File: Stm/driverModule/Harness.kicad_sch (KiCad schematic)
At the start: 2 parts, among them J1 346916080, J3 346916080

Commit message: Update
Add connection to the harness
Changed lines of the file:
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@@
-	(wire
-		(pts
-			(xy 124.46 107.95) (xy 129.54 107.95)
-		)
-		(stroke
-			(width 0)
-			(type default)
-		)
-	)
 	(wire
 		(pts
@@
 	(wire
 		(pts
+			(xy 129.54 107.95) (xy 124.46 107.95)
+		)
+		(stroke
+			(width 0)
+			(type default)
+		)
+	)
+	(wire
+		(pts
 			(xy 124.46 62.23) (xy 129.54 62.23)
+		)
+		(stroke
+			(width 0)
+			(type default)
+		)
+	)
+	(wire
+		(pts
+			(xy 129.54 113.03) (xy 129.54 107.95)
 		)
 		(stroke
@@
 	(hierarchical_label "LIN_BUS"
 		(shape bidirectional)
-		(at 186.69 90.17 0)
+		(at 87.63 86.36 0)
 		(effects
 			(font
@@
 		(shape output)
 		(at 129.54 74.93 0)
+		(effects
+			(font
+				(size 1.27 1.27)
+			)
+			(justify left)
+		)
+	)
+	(hierarchical_label "GND"
+		(shape bidirectional)
+		(at 129.54 107.95 0)
 		(effects
 			(font
@@
 	(symbol
 		(lib_id "power:GND")
-		(at 129.54 107.95 0)
+		(at 129.54 113.03 0)
 		(unit 1)
 		(exclude_from_sim no)
@@
 		(fields_autoplaced yes)
 		(property "Reference" "#PWR019"
-			(at 129.54 114.3 0)
+			(at 129.54 119.38 0)
 			(effects
 				(font
@@
 		)
 		(property "Value" "GND"
+			(at 129.54 118.11 0)
+			(effects
+				(font
+					(size 1.27 1.27)
+				)
+			)
+		)
+		(property "Footprint" ""
 			(at 129.54 113.03 0)
 			(effects
@@
 					(size 1.27 1.27)
 				)
-			)
-		)
-		(property "Footprint" ""
-			(at 129.54 107.95 0)
-			(effects
-				(font
-					(size 1.27 1.27)
-				)
 				(hide yes)
 			)
 		)
 		(property "Datasheet" ""
-			(at 129.54 107.95 0)
+			(at 129.54 113.03 0)
 			(effects
 				(font
@@
 		)
 		(property "Description" "Power symbol creates a global label with name \"GND\" , ground"
-			(at 129.54 107.95 0)
-			(effects
-				(font
+			(at 129.54 113.03 0)
+			(effects
+				(font

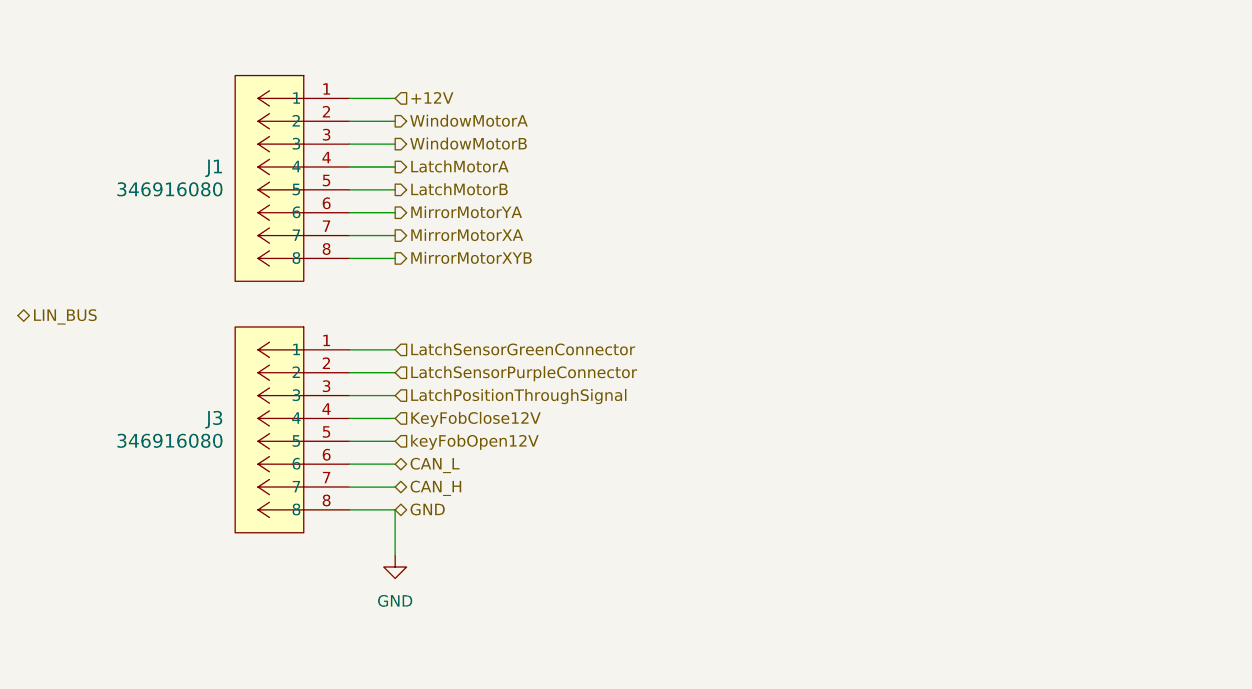
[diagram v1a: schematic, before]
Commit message: libraries
Add new molex connectors
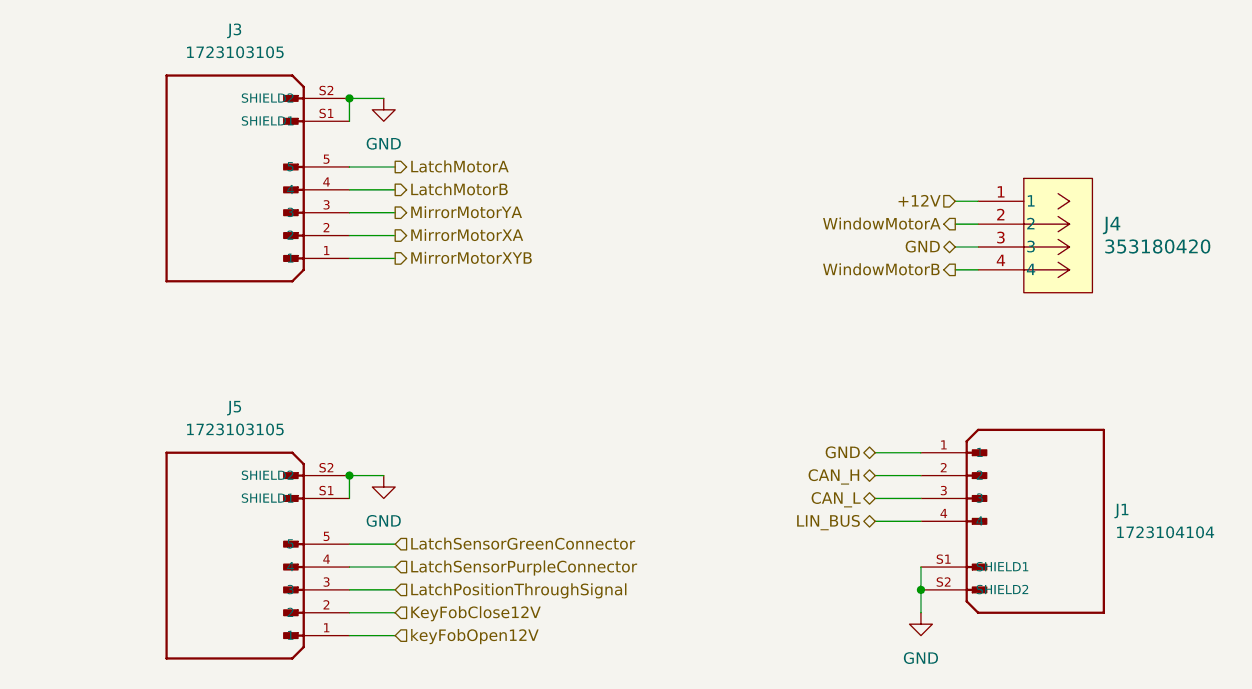
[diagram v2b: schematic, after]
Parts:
- removed J1, J3: 346916080, User_Footprint:CONN_SD-34691-601_08_MOL, symbol _Connectors:346916080
- added J1: 1723104104, User_Footprint:MOLEX_1723104104, symbol _Connectors:1723104104
- added J3, J5: 1723103105, User_Footprint:MOLEX_1723103105, symbol _Connectors:1723103105
- added J4: 353180420, User_Footprint:CONN_35318-0420_MOL, symbol _Misc_Symbols:353180420
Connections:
- net +12V: now also J4.1
- net CAN_H: now also J1.2
- net CAN_L: now also J1.3
- net GND: now also J1.1, J1.S1 (SHIELD1), J1.S2 (SHIELD2), J3.S1 (SHIELD1), J3.S2 (SHIELD2), J4.3, J5.S1 (SHIELD1), J5.S2 (SHIELD2)
- net KeyFobClose12V: now also J5.2
- net LIN_BUS: now also J1.4
- net LatchMotorA: now also J3.5
- net LatchMotorB: now also J3.4
- net LatchPositionThroughSignal: now also J5.3
- net LatchSensorGreenConnector: now also J5.5
- net LatchSensorPurpleConnector: now also J5.4
- net MirrorMotorXA: now also J3.2
- net MirrorMotorXYB: now also J3.1
- net MirrorMotorYA: now also J3.3
- net WindowMotorA: now also J4.2
- net WindowMotorB: now also J4.4
- net keyFobOpen12V: now also J5.1

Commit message: routing
Finished PCB routing
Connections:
- net LatchMotorA: now also J3.4; no longer J3.5
- net LatchMotorB: now also J3.5; no longer J3.4
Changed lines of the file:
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@@
+	(wire
+		(pts
+			(xy 124.46 116.84) (xy 129.54 116.84)
+		)
+		(stroke
+			(width 0)
+			(type default)
+		)
+	)
+	(wire
+		(pts
+			(xy 191.77 73.66) (xy 194.31 73.66)
+		)
+		(stroke
+			(width 0)
+			(type default)
+		)
+	)
+	(wire
+		(pts
+			(xy 187.96 116.84) (xy 187.96 114.3)
+		)
+		(stroke
+			(width 0)
+			(type default)
+		)
+	)
+	(wire
+		(pts
+			(xy 124.46 114.3) (xy 129.54 114.3)
+		)
+		(stroke
+			(width 0)
+			(type default)
+		)
+	)
+	(wire
+		(pts
+			(xy 124.46 77.47) (xy 129.54 77.47)
+		)
+		(stroke
+			(width 0)
+			(type default)
+		)
+	)
+	(wire
+		(pts
+			(xy 187.96 106.68) (xy 182.88 106.68)
+		)
+		(stroke
+			(width 0)
+			(type default)
+		)
+	)
+	(wire
+		(pts
+			(xy 124.46 80.01) (xy 129.54 80.01)
+		)
+		(stroke
+			(width 0)
+			(type default)
+		)
+	)
+	(wire
+		(pts
+			(xy 124.46 119.38) (xy 129.54 119.38)
+		)
+		(stroke
+			(width 0)
+			(type default)
+		)
+	)
+	(wire
+		(pts
+			(xy 124.46 62.23) (xy 124.46 64.77)
+		)
+		(stroke
+			(width 0)
+			(type default)
+		)
+	)
 	(wire
 		(pts
@@
 	(wire
 		(pts
-			(xy 124.46 116.84) (xy 129.54 116.84)
-		)
-		(stroke
-			(width 0)
-			(type default)
-		)
-	)
-	(wire
-		(pts
-			(xy 191.77 73.66) (xy 194.31 73.66)
-		)
-		(stroke
-			(width 0)
-			(type default)
-		)
-	)
-	(wire
-		(pts
-			(xy 187.96 116.84) (xy 187.96 114.3)
-		)
-		(stroke
-			(width 0)
-			(type default)
-		)
-	)
-	(wire
-		(pts
-			(xy 124.46 114.3) (xy 129.54 114.3)
-		)
-		(stroke
-			(width 0)
-			(type default)
-		)
-	)
-	(wire
-		(pts
-			(xy 124.46 77.47) (xy 129.54 77.47)
-		)
-		(stroke
-			(width 0)
-			(type default)
-		)
-	)
-	(wire
-		(pts
-			(xy 187.96 106.68) (xy 182.88 106.68)
-		)
-		(stroke
-			(width 0)
-			(type default)
-		)
-	)
-	(wire
-		(pts
-			(xy 124.46 80.01) (xy 129.54 80.01)
-		)
-		(stroke
-			(width 0)
-			(type default)
-		)
-	)
-	(wire
-		(pts
-			(xy 124.46 119.38) (xy 129.54 119.38)
-		)
-		(stroke
-			(width 0)
-			(type default)
-		)
-	)
-	(wire
-		(pts
-			(xy 124.46 62.23) (xy 124.46 64.77)
-		)
-		(stroke
-			(width 0)
-			(type default)
-		)
-	)
-	(wire
-		(pts
 			(xy 187.96 104.14) (xy 182.88 104.14)
 		)
@@
 	(wire
 		(pts
+			(xy 182.88 101.6) (xy 187.96 101.6)
+		)
+		(stroke
+			(width 0)
+			(type default)
+		)
+	)
+	(wire
+		(pts
+			(xy 124.46 104.14) (xy 124.46 106.68)
+		)
+		(stroke
+			(width 0)
+			(type default)
+		)
+	)
+	(wire
+		(pts
+			(xy 187.96 119.38) (xy 187.96 116.84)
+		)
+		(stroke
+			(width 0)
+			(type default)
+		)
+	)
+	(wire
+		(pts
+			(xy 191.77 81.28) (xy 194.31 81.28)
+		)
+		(stroke
+			(width 0)
+			(type default)
+		)
+	)
+	(wire
+		(pts
 			(xy 124.46 69.85) (xy 129.54 69.85)
 		)
@@
 	(wire
 		(pts
-			(xy 182.88 101.6) (xy 187.96 101.6)
-		)
-		(stroke
-			(width 0)
-			(type default)
-		)
-	)
-	(wire
-		(pts
-			(xy 124.46 104.14) (xy 124.46 106.68)
-		)
-		(stroke
-			(width 0)
-			(type default)
-		)
-	)
-	(wire
-		(pts
-			(xy 187.96 119.38) (xy 187.96 116.84)
-		)
-		(stroke
-			(width 0)
-			(type default)
-		)
-	)
-	(wire
-		(pts
-			(xy 191.77 81.28) (xy 194.31 81.28)
-		)
-		(stroke
-			(width 0)
-			(type default)
-		)
-	)
-	(wire
-		(pts
 			(xy 124.46 74.93) (xy 129.54 74.93)
 		)
@@
 	(hierarchical_label "LatchMotorA"
 		(shape output)
+		(at 129.54 72.39 0)
+		(effects
+			(font
+				(size 1.27 1.27)
+			)
+			(justify left)
+		)
+	)
+	(hierarchical_label "LIN_BUS"
+		(shape bidirectional)
+		(at 182.88 109.22 180)
+		(effects
+			(font
+				(size 1.27 1.27)
+			)
+			(justify right)
+		)
+	)
+	(hierarchical_label "MirrorMotorYA"
+		(shape output)
+		(at 129.54 74.93 0)
+		(effects
+			(font
+				(size 1.27 1.27)
+			)
+			(justify left)
+		)
+	)
+	(hierarchical_label "GND"
+		(shape bidirectional)
+		(at 182.88 101.6 180)
+		(effects
+			(font
+				(size 1.27 1.27)
+			)
+			(justify right)
+		)
+	)
+	(hierarchical_label "LatchMotorB"
+		(shape output)
 		(at 129.54 69.85 0)
 		(effects
 			(font
-				(size 1.27 1.27)
-			)
-			(justify left)
-		)
-	)
-	(hierarchical_label "LIN_BUS"
-		(shape bidirectional)
-		(at 182.88 109.22 180)
-		(effects
-			(font
-				(size 1.27 1.27)
-			)
-			(justify right)
-		)
-	)
-	(hierarchical_label "MirrorMotorYA"
-		(shape output)
-		(at 129.54 74.93 0)
-		(effects
-			(font
-				(size 1.27 1.27)
-			)
-			(justify left)
-		)
-	)
-	(hierarchical_label "GND"
-		(shape bidirectional)
-		(at 182.88 101.6 180)
-		(effects
-			(font
-				(size 1.27 1.27)
-			)
-			(justify right)
-		)
-	)
-	(hierarchical_label "LatchMotorB"
-		(shape output)
-		(at 129.54 72.39 0)
-		(effects
-			(font
